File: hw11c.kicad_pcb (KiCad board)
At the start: 2 copper layers, 49 x 27.5 mm, 72 parts, among them Q1 KX-7_12MHZ, SW1 BUTT1, SW2 BUTT2, X1 ~RESET, X10 PIO2.8, X11 PIO1.4, X12 ADC3, X13 PIO0.8, X14 PIO0.9, X15 MAT0, X16 PIO0.6, X17 PIO0.7, X2 SWCLK, X3 SWDIO, X4 SSEL1, X5 SCK1, X6 MISO1, X7 MOSI1, X8 PIO2.6, X9 PIO2.7

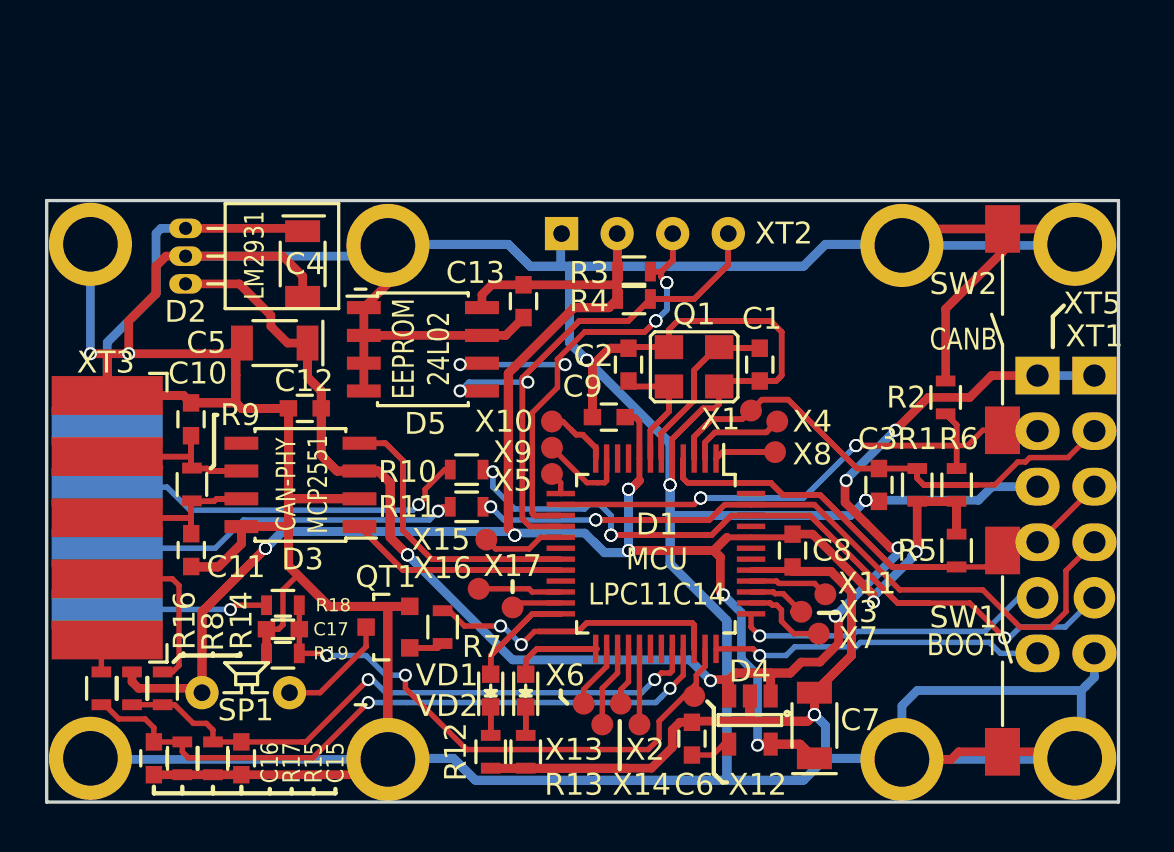
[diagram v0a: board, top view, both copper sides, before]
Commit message: Add fault-tolerance CAN PHY: TJA1055. Version of board 2.1.
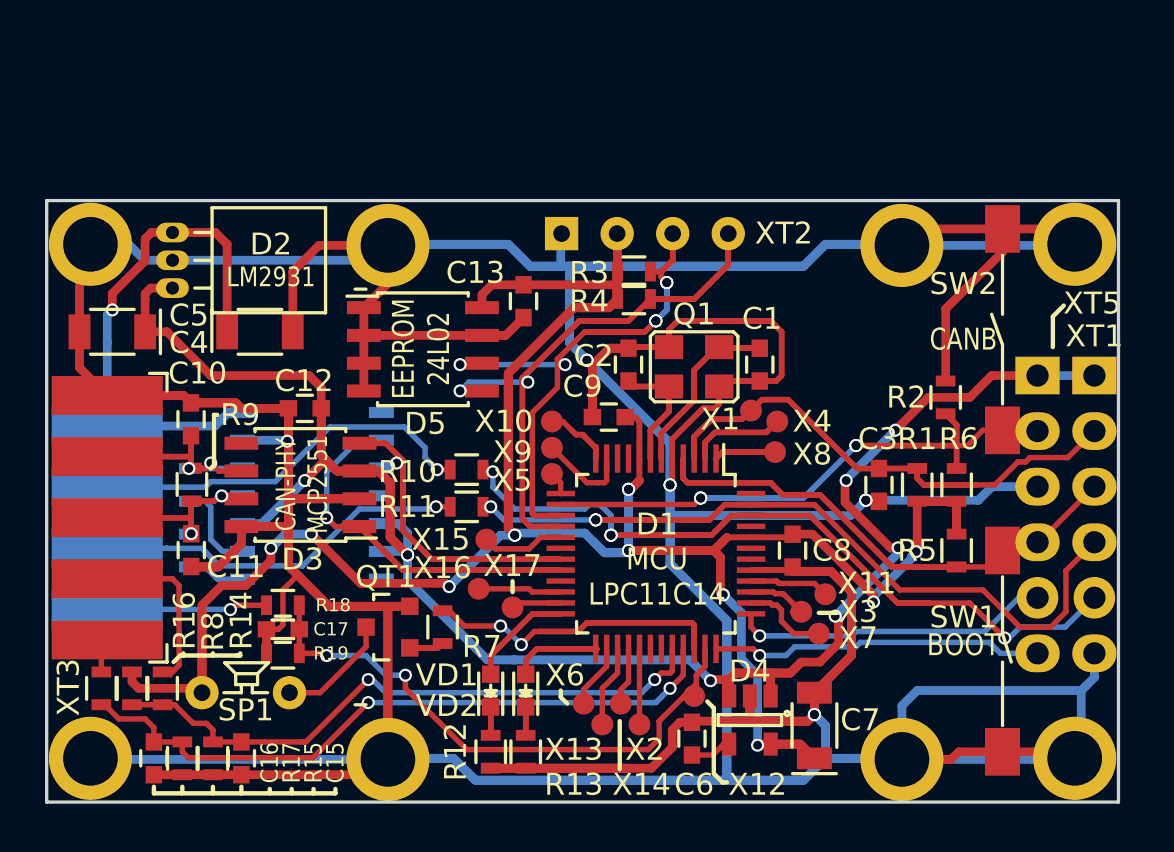
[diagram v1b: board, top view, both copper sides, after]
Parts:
- added D6: TJA1055, libs:SOIC-14_N, B.Cu at (61.9, 63.5)
- added R20: 5.6k, libs:R_0603, B.Cu at (56.4, 63.0)
- added R21: 5.6k, libs:R_0603, B.Cu at (56.4, 66.0)
- moved C5 7.44 mm to (52.9, 56.0)
- moved C4 3.66 mm to (59.6, 56.0), turned to 0 degrees
- moved D2 0.63 mm to (55.6, 54.0)
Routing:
- net /3.3V: track 154.1 -> 141.0 mm, vias 12 -> 13
- net GND: track 504.6 -> 494.2 mm, vias 10 -> 9
- net /5V: track 85.7 -> 94.8 mm, vias 7 -> 8
- net /12V: track 17.0 -> 24.3 mm, vias 0 -> 1
- net /CAN_TX: track 20.1 -> 26.9 mm, vias 0 -> 1
- net Net-(D6-Pad9): track 0.00 -> 4.28 mm
- net Net-(D6-Pad8): track 0.00 -> 2.68 mm
- net /CANL: track 25.0 -> 26.2 mm, vias 0 -> 2
- net /CANH: track 20.2 -> 21.4 mm, vias 0 -> 2
- net /CAN_RX: track 26.5 -> 27.6 mm, vias 0 -> 1
- net Net-(R10-Pad1): track 17.1 -> 17.9 mm
- net Net-(R11-Pad1): track 16.5 -> 17.1 mm
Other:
- board text added: "igorkov / BCOMP11 igorkov.org/bcomp11v2 2018 / version 2.1"
- board text removed: "igorkov / BCOMP11 igorkov.org/bcomp11v2 2018 / version 2.0"

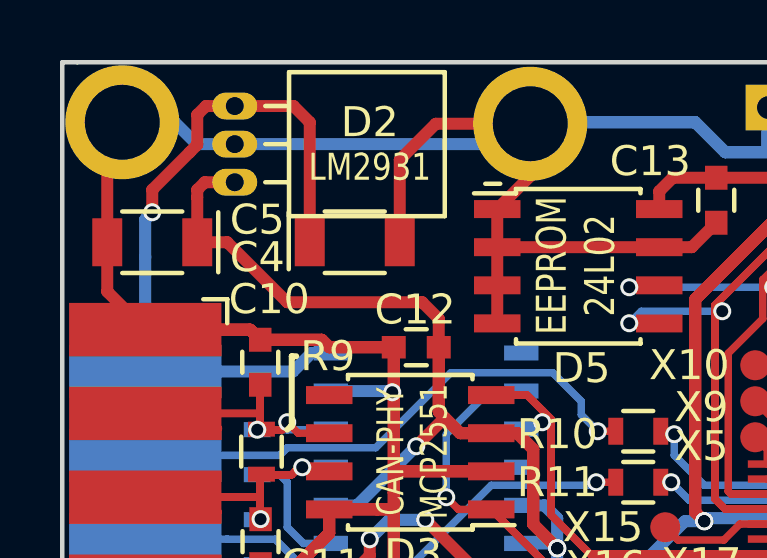
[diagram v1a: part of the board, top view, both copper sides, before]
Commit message: Fix C5 position.
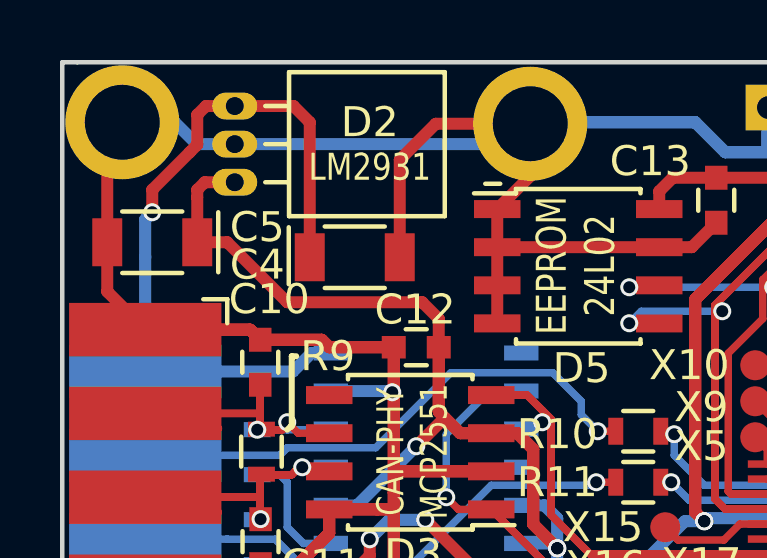
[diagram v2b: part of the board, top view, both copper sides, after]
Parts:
- moved C4 0.50 mm to (59.6, 56.5)
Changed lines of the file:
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@@
     (links 161)
     (no_connects 0)
-    (area 49.824999 49.924999 98.975001 77.575001)
+    (area 49.527143 49.605 117.971429 90.700001)
     (thickness 1.6)
     (drawings 49)
@@
     (tags "capacitor 1206")
     (attr smd)
-    (fp_text reference C5 (at -3.5 0.75 360) (layer F.SilkS)
+    (fp_text reference C5 (at -3.5 0.5 360) (layer F.SilkS)
       (effects (font (size 1 1) (thickness 0.15)))
     )
@@
   )
   (module libs:C_1206 (layer F.Cu)
-    (at 59.65 56)
+    (at 59.65 56.5)
     (descr "Capacitor SMD 1206, reflow soldering, AVX (see smccp.pdf)")
     (tags "capacitor 1206")
     (attr smd)
-    (fp_text reference C4 (at -3.25 0.5) (layer F.SilkS)
-      (effects (font (size 1 1) (thickness 0.15)))
-    )
+    (fp_text reference C4 (at -3.25 0.25) (layer F.SilkS)
+      (effects (font (size 1 1) (thickness 0.15)))
+    )

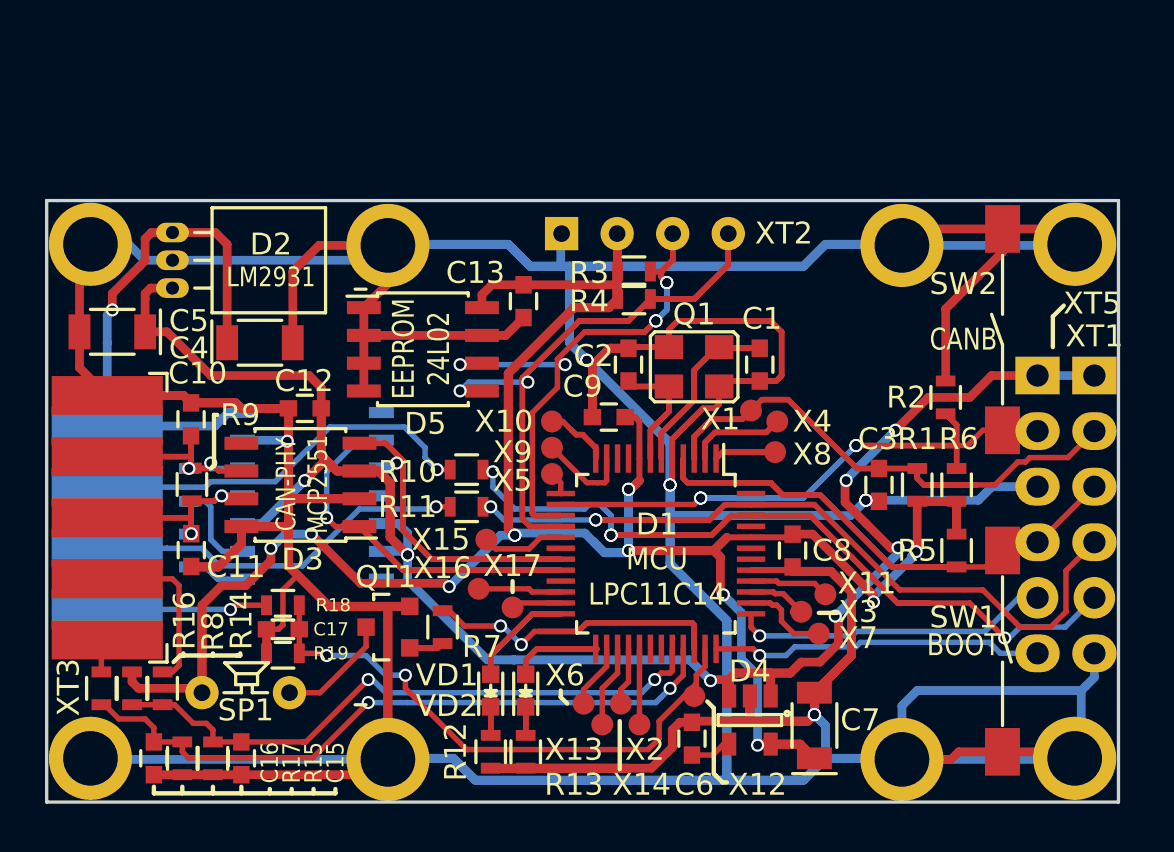
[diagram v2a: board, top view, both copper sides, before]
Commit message: Add open-drain outs (shared with analog input). Version 2.3.
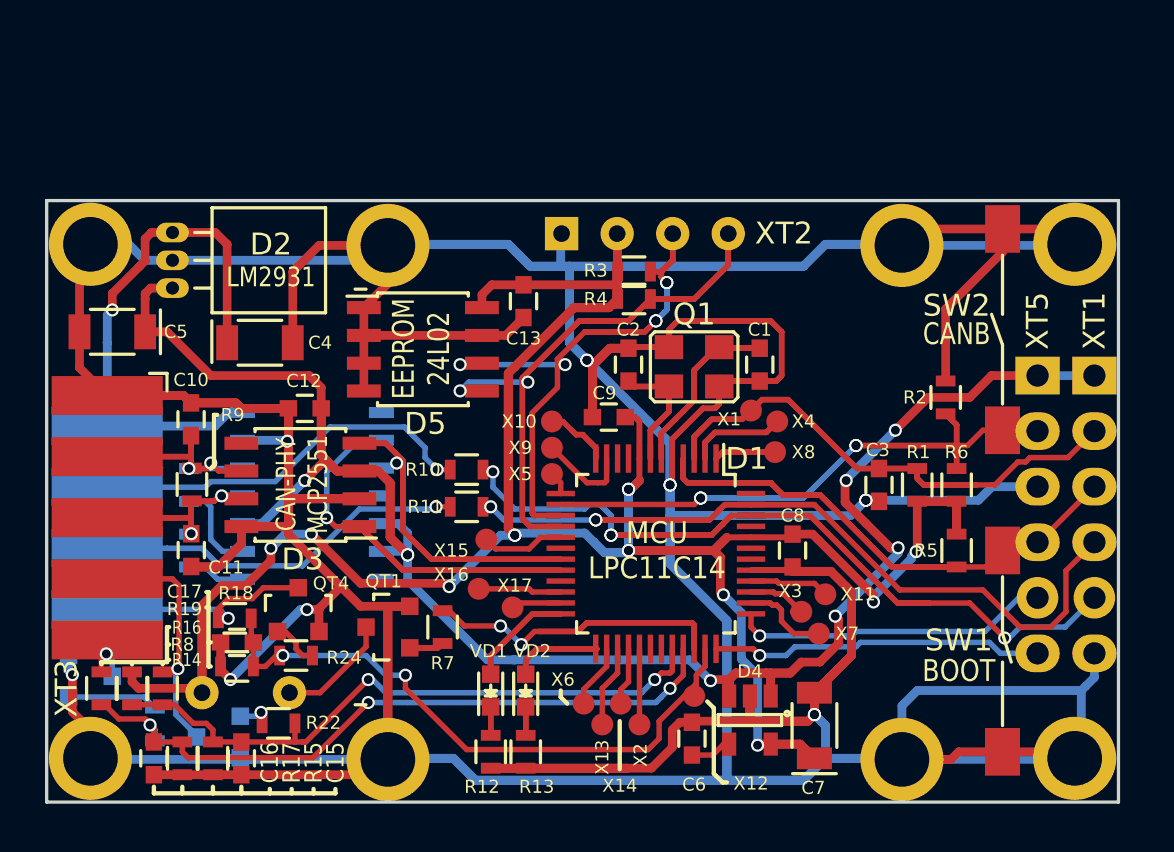
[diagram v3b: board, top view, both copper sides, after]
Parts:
- added QT2: BC817, libs:SOT-23, B.Cu at (57.8, 74.5)
- added QT3: BC817, libs:SOT-23, B.Cu at (51.9, 71.8)
- added QT4: BC817, libs:SOT-23, F.Cu at (61.4, 68.7)
- added R22: 4.7k, libs:R_0603, F.Cu at (60.5, 73.9)
- added R23: 4.7k, libs:R_0603, B.Cu at (54.9, 74.0)
- added R24: 4.7k, libs:R_0603, F.Cu at (61.3, 70.8)
- SP1: moved to B.Cu
- moved R18 2.28 mm to (58.5, 69.1)
- moved C17 2.18 mm to (58.6, 70.2)
- moved R19 2.18 mm to (58.6, 71.3)
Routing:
- net Net-(QT3-Pad1): track 0.00 -> 4.16 mm
- net /AN1: track 7.93 -> 11.6 mm, vias 0 -> 1
- net /AN3: track 7.37 -> 10.6 mm
- net GND: track 494.2 -> 497.1 mm, vias 9 -> 12
- net /ADC3: track 27.0 -> 29.4 mm
- net Net-(QT4-Pad1): track 0.00 -> 2.23 mm
- net /AN2: track 1.57 -> 3.37 mm, vias 0 -> 1
- net Net-(QT2-Pad1): track 0.00 -> 1.54 mm, vias 0 -> 1
- net /ADC1: track 31.0 -> 31.9 mm, vias 2 -> 3
- net /ADC0: track 28.6 -> 29.4 mm
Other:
- board text added: "igorkov / BCOMP11 igorkov.org/bcomp11v2 2018 / version 2.3"
- board text removed: "igorkov / BCOMP11 igorkov.org/bcomp11v2 2018 / version 2.1"

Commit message: Fix silk layer. Add wiki links.
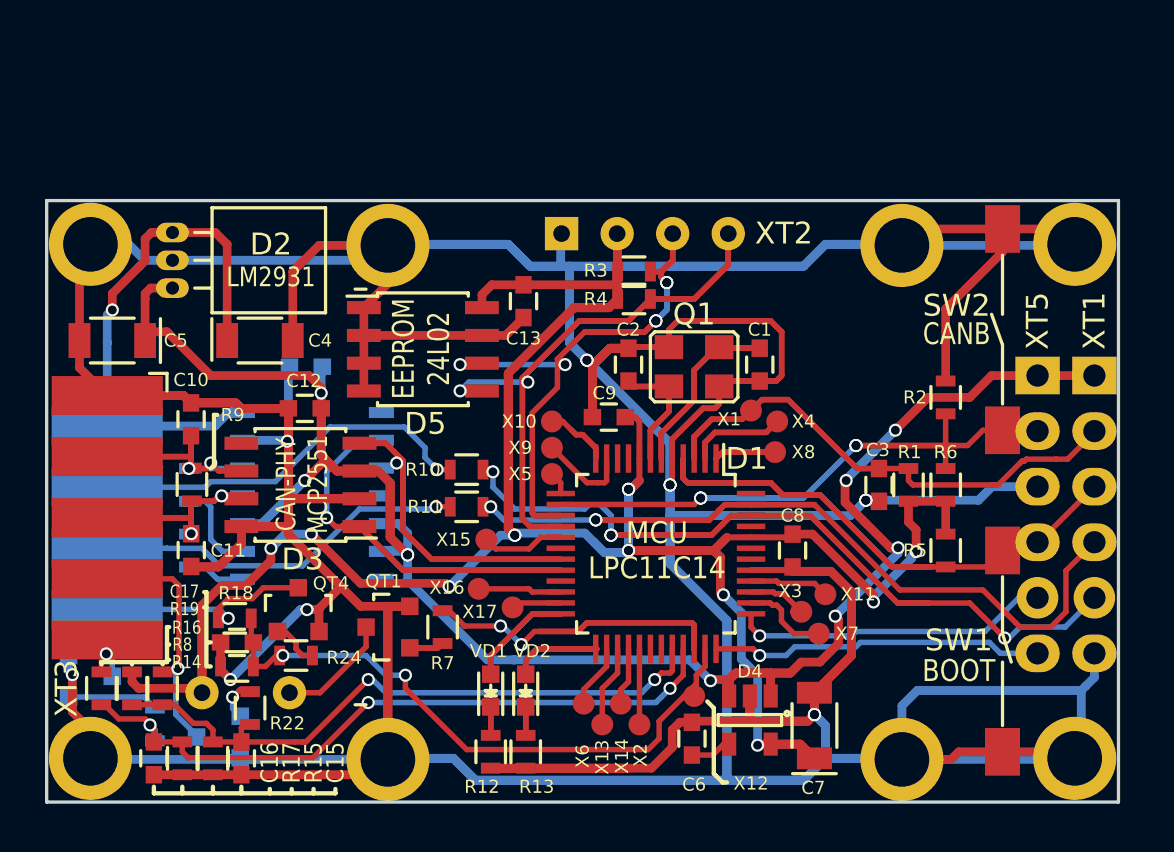
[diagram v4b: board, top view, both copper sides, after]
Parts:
- added C14: 0.1, libs:C_0603, B.Cu at (61.8, 57.6)
- moved R22 1.48 mm to (59.2, 73.2), turned to 270 degrees
- moved R5 0.50 mm to (91.0, 66.0)
- moved R6 0.50 mm to (91.0, 63.0)
- moved R1 0.40 mm to (89.3, 63.0)
- moved C5 0.40 mm to (52.9, 56.4)
- moved C4 0.10 mm to (59.6, 56.4)
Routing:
- net /~RESET: track 40.5 -> 34.9 mm
- net /3.3V: track 141.0 -> 137.7 mm
- net GND: track 497.1 -> 500.2 mm
- net /BUTT2: track 41.4 -> 38.5 mm
- net /BOOT: track 38.5 -> 36.9 mm
- net /5V: track 94.8 -> 96.0 mm, vias 8 -> 9
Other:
- board text added: "FT CAN-PHY TJA1055"

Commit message: Fix SO-14 case for TJA-1055.
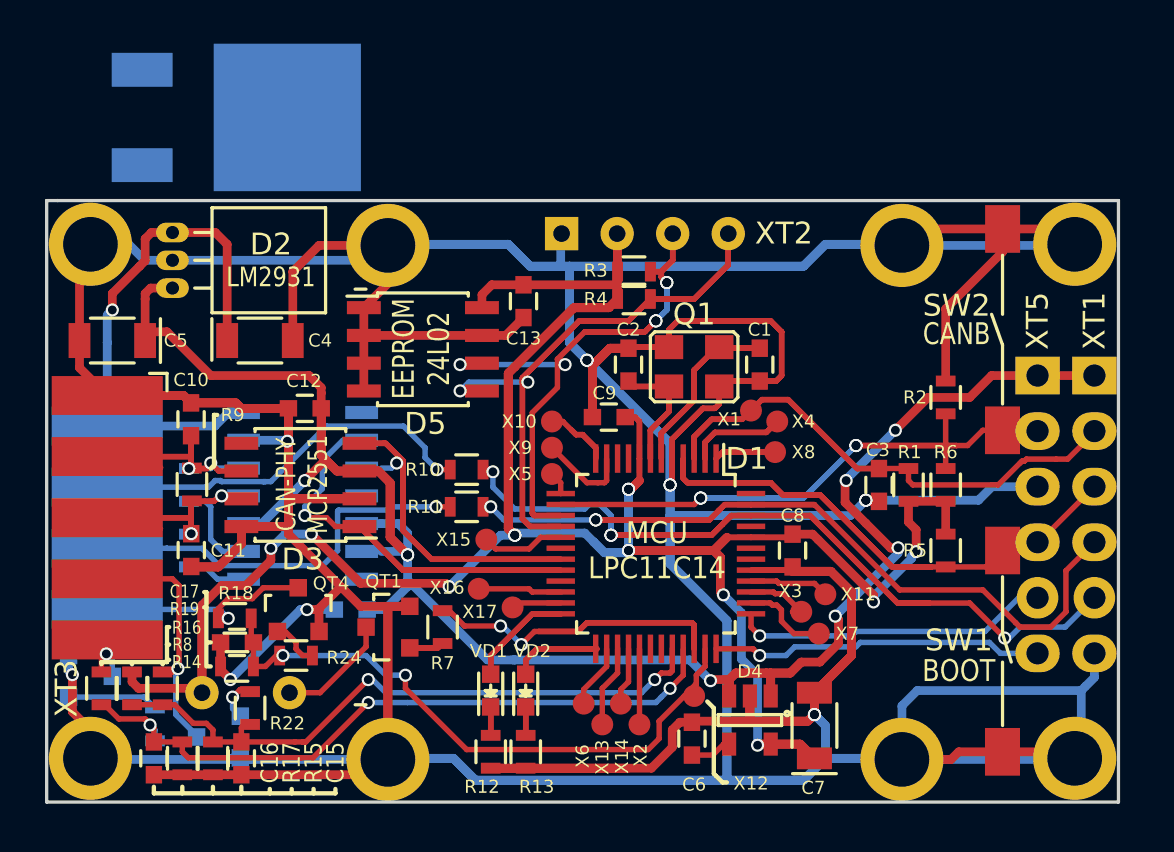
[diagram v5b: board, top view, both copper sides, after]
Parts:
- added D7: 78M05, libs:D-Pak_TO252AA, B.Cu at (58.6, 46.2)
- D6: footprint libs:SOIC-14_N -> libs:SOIC-14_3.9x8.7mm_Pitch1.27mm
- moved C14 11.3 mm to (63.8, 68.7)
- moved D6 0.30 mm to (61.6, 63.5), turned to 180 degrees
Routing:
- net /5V: track 96.0 -> 98.3 mm, vias 9 -> 8
- net GND: track 500.2 -> 498.3 mm
- net Net-(R11-Pad1): track 17.1 -> 18.3 mm
- net /CAN_TX: track 26.9 -> 27.8 mm
